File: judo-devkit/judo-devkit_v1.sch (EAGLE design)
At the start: 24 parts

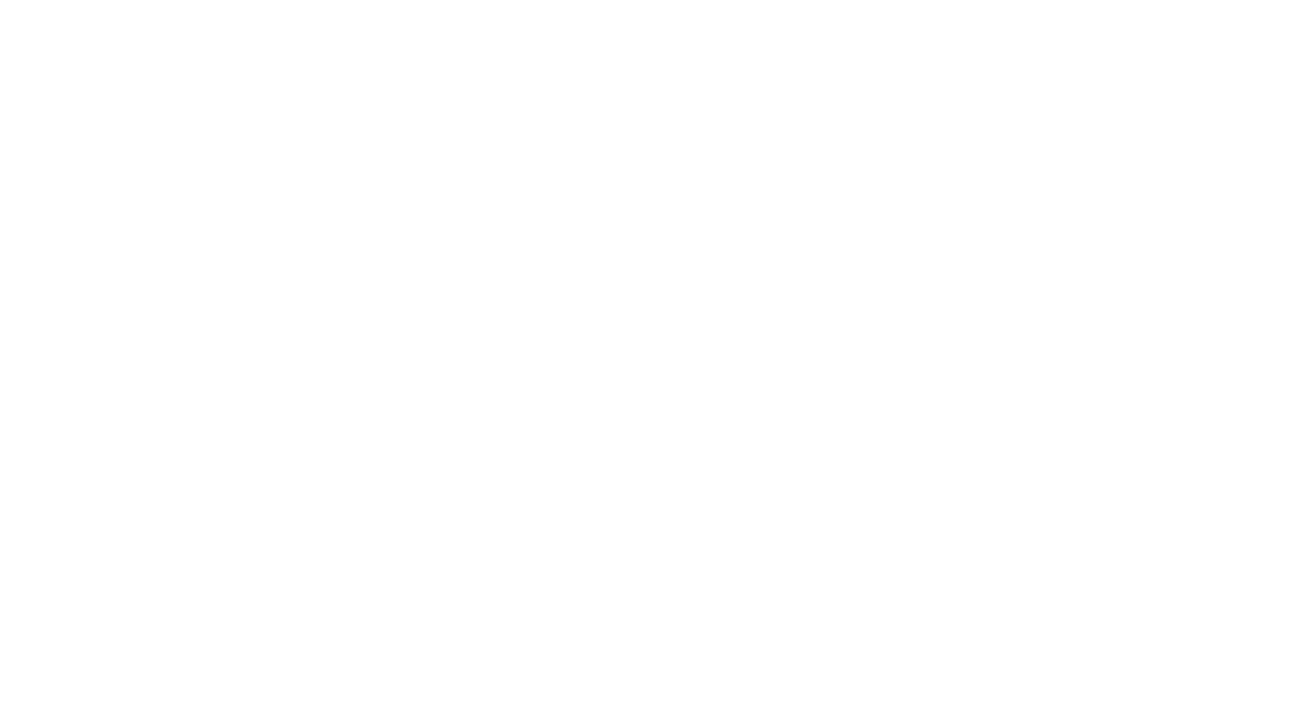
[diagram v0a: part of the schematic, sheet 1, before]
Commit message: added apollo3, power management
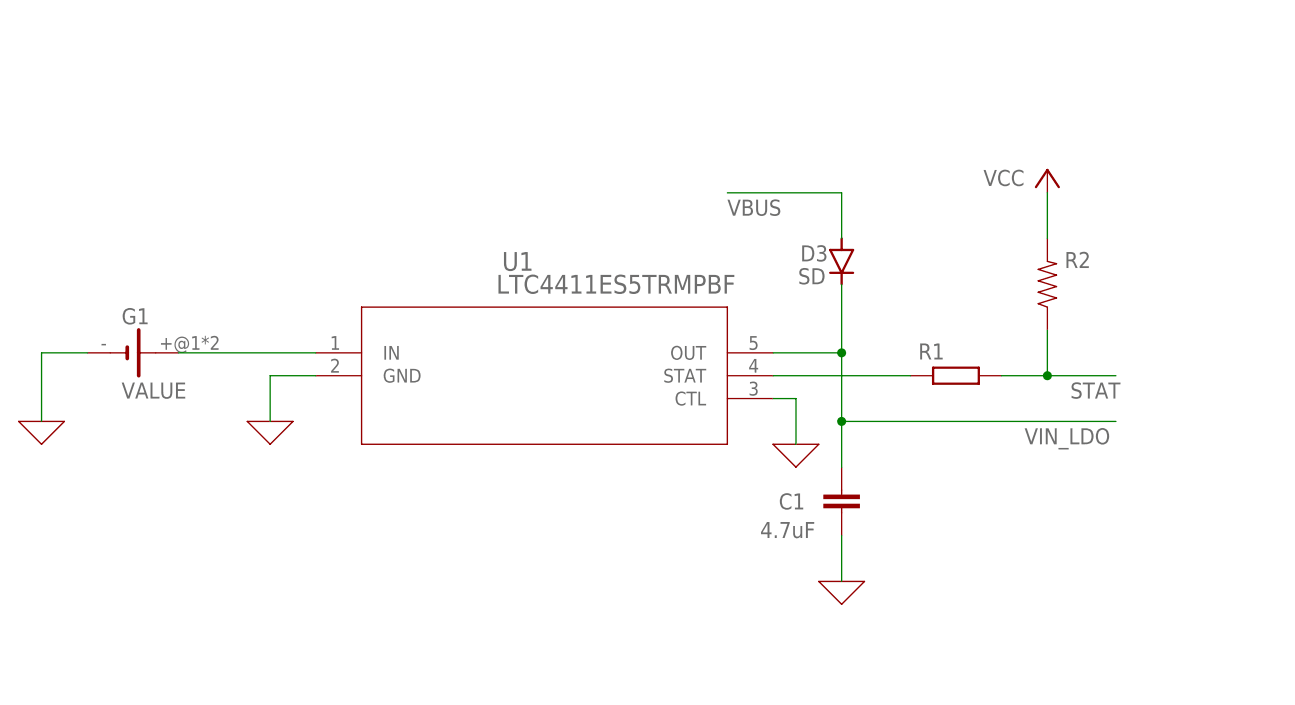
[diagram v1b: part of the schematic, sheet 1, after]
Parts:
- added C1: 4.7uF, Moo1.2:CAPACITOR
- added C13, C4: 15pF, SparkFun-Capacitors:15PF-0603-50V-5%
- added C14, C19: 0.1uF, SparkFun-Capacitors:0.1UF-0402T-16V-10%
- added C17: 10nF, SparkFun-Capacitors:10NF-0603-50V-10%
- added C18: 0.1uF, SparkFun-Capacitors:0.1UF-0603-25V-(+80/-20%)
- added C2, C23, C3: 1.0uF, SparkFun-Capacitors:1.0UF-0402T-16V-10%
- added C20, C21: 0.1uF, SparkFun-Capacitors:0.1UF-0603-25V-5%
- added C22: 10uF, SparkFun-Capacitors:10UF-0603-6.3V-20%
- added C28: 1nF, SparkFun-Capacitors:1.0NF/1000PF-0603-50V-10%
- added C5, C6: 4.7uF, SparkFun-Capacitors:4.7UF-0603-6.3V-(10%)
- added D10: GREEN, SparkFun-LED:LED-GREEN0603
- added D3: SD, diode:1N4148DO35-7
- added D4, D9: Yellow, SparkFun-LED:LED-YELLOW0603
- added D5, D7: 1A/23V/620mV, SparkFun-DiscreteSemi:DIODE-SCHOTTKY-BAT20J
- added D6: RED, SparkFun-LED:LED-RED0603
- added D8: BLUE, SparkFun-LED:LED-BLUE0603
- added E1: SPH0641LM4H, SparkFun-Sensors:SPH0641LM4H-1_MICROPHONE
- added FD1, FD2, FD3, FD4: FIDUCIALUFIDUCIAL, SparkFun-Aesthetics:FIDUCIALUFIDUCIAL
- added G1: 10MM_SM_COIN_CELL_CLIP, battery:10MM_SM_COIN_CELL_CLIP
- added J1: (no value), SparkFun-Connectors:JST_2MM_MALE
- added J10: USB Female Type C Connector, SparkFun-Connectors:USB_C4-LAYER-ISOLATED
- added J11: CORTEX_DEBUG, SparkFun-Connectors:CORTEX_JTAG_DEBUG_MINIMUM_PTH_NS
- added J12, J14, J4, J5: (no value), SparkFun-Connectors:CONN_021X02_NO_SILK
- added J13, J2: (no value), SparkFun-Connectors:CONN_12NO_SILK
- added J3: (no value), SparkFun-Connectors:QWIIC_CONNECTORJS-1MM
- added J7, J9: (no value), SparkFun-Connectors:CONN_07NO_SILK
- added R1: (no value), rcl:R-EU_R0402
- added R15, R16, R3, R6, R7: 1k, SparkFun-Resistors:1KOHM-0603-1/10W-1%
- added R17, R18: 5.1k, SparkFun-Resistors:5.1KOHM5.1KOHM-0603-1/10W-1%
- added R19: 220k, SparkFun-Resistors:220KOHM-0603-1/10W-1%
- added R2: (no value), SparkFun-Resistors:RESISTOR0805-RES
- added R20: DNP, SparkFun-Resistors:DNP-0603
- added R21: 100k, SparkFun-Resistors:100KOHM-0603-1/10W-1%
- added R4: 10k, SparkFun-Resistors:10KOHM-0603-1/10W-1%
- added R5: 2.0k, SparkFun-Resistors:2.0KOHM-0603-1/10W-5%
- added S1: RESET, SparkFun-Switches:MOMENTARY-SWITCH-SPST-SMD-4.6X2.8MM
- added TP1, TP2, TP3, TP4, TP5, TP6: TEST-POINT3X5, SparkFun-Connectors:TEST-POINT3X5
- added U1: LTC4411ES5TRMPBF, ltc4411:LTC4411ES5TRMPBF
- added U2: MCP73831, SparkFun-IC-Power:MCP73831
- added U3: 3.3V, SparkFun-IC-Power:V_REG_AP2112K-3.3V
- added U4: ARTEMIS_MODULESMD, SparkFun-IC-Microcontroller:ARTEMIS_MODULESMD
- added U6: CH340E_MSOP10, SparkFun-IC-Comms:CH340E_MSOP10
- added Y2: 32.768kHz, SparkFun-Clocks:CRYSTAL-32.768KHZSMD-3.2X1.5
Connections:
- new net !RESET: C20.2, C28.1, J11.!RESET, J2.10, R21.1, S1.2, U4.!RST
- new net !RTS: C20.1, C21.1, R20.2, U6.!RTS
- new net 10: J2.2, U4.(SDA4/MISO4/RX1)D40
- new net 3.3V: C14.1, C17.1, C18.1, C19.2, C22.1, C23.1, C3.1, E1.SEL, E1.VDD, J11.VCC, J2.9, J3.2, R15.2, R21.2, R3.2, R7.2, U3.OUT, U4.VDD*2, U6.V3, U6.VCC
- new net 8: J7.1, U4.(MOSI3/RX1)D38
- new net BOOT: C21.2, R19.2, U4.~BOOT(MOSI5/RX1/32KHZ)
- new net CC1: J10.CC1, R18.2
- new net CC2: J10.CC2, R17.2
- new net D+1: J10.D+, U6.UD+
- new net D-1: J10.D-, U6.UD-
- new net GND: C13.1, C14.2, C17.2, C18.2, C19.1, C2.2, C22.2, C23.2, C28.2, C3.2, C4.1, C5.2, C6.2, D6.C, D8.C, E1.GND, J1.-, J10.GND, J11.GND, J12.1, J13.1, J13.10, J13.11, J13.12, J13.2, J13.3, J13.4, J13.5, J13.6, J13.7, J13.8, J13.9, J14.1, J14.2, J2.11, J3.1, J4.2, J9.1, J9.2, J9.3, J9.4, J9.5, J9.6, J9.7, R17.1, R18.1, R19.1, R20.1, R5.1, S1.1, U2.VSS, U3.GND, U4.GND*6, U6.GND
- new net N$1: G1.+, U1.IN
- new net N$10: D6.A, R3.1
- new net N$11: D10.A, R7.1
- new net N$12: D9.A, R15.1
- new net N$2: R5.2, U2.PROG
- new net N$3: R1.2, U1.STAT
- new net N$4: D4.C, R6.2
- new net N$6: R6.1, U2.STAT
- new net N$7: C4.2, U4.XO, Y2.2
- new net N$8: C13.2, U4.XI, Y2.1
- new net N$9: D8.A, R16.1
- new net PDMCLK: E1.CLK, U4.(TX1/PDMCLK/SCCIO)~D37
- new net PDMDATA: E1.DATA, U4.(RX1/TRIG1/PDMDATA)D36
- new net RXI-0: D9.C, TP5.1, U4.~D49(RX0/SDA5/MISO5), U6.TXO
- new net SHLD: J10.SHLD
- new net STAT: R1.1, R2.1
- new net SWDCK: J11.SWDCLK, TP1.1, U4.D20(SWDCK/TX1)
- new net SWDIO: J11.SWDIO, TP2.1, U4.D21(SWDIO/RX1/SCCRST)
- new net TXO-0: D10.C, TP6.1, U4.~D48(TX0/SCL5/SCK5), U6.RXI
- new net VBUS: D3.A
- new net VCC: R2.2
- new net VIN: C2.1, D5.C, D7.C, J2.12, R4.2, U3.IN
- new net VIN_LDO: C1.2, D3.C, U1.OUT
- new net VREG_EN: J4.1, R4.1, U3.EN
- new net V_BATT: C6.1, D7.A, J1.+, J12.2, U2.VBAT
- new net V_USB: C5.1, D4.A, D5.A, J10.VBUS, U2.VIN
- new net ~11: J2.3, U4.(SCL0/SCK0)~D5
- new net ~12: J2.4, U4.(MOSI0/CLKOUT)~D7
- new net ~13: J2.5, U4.(SDA0/MISO0/I2SDAT)~D6
- new net ~4: J7.5, U4.(CMPIN1/SCCIO)~D18
- new net ~6: J7.3, U4.(SDA3/MISO3/RX1)~D43
- new net ~7: J7.2, U4.(SCL3/SCK3/TX1)~D42
- new net ~9: J2.1, U4.(SCL4/SCK4/TX1)~D39
- new net ~A0: J5.2, U4.~AD13(I2SBCLK/RX1)
- new net ~A1: J11.SWO, J5.1, U4.~AD33(SWO/32KHZ)
- new net ~A14: J2.6, U4.~AD35(TX1/I2SDAT/PDMCLK)
- new net ~A15: J2.7, U4.~AD32(SCCIO)
- new net ~A16: J2.8, U4.~AD12(PDMCLK/TX1)
- new net ~A2: J7.7, U4.~AD11(PDMDATA)
- new net ~A3: J7.6, U4.~AD29(PDMDATA)
- new net ~A5: J7.4, U4.~AD31(SCCCLK)
- new net ~D19/LED: R16.2, U4.(CMPRF0/SCCCLK/I2SBCLK)~D19
- new net ~D25/SDA2: J3.3, TP3.1, U4.(SDA2/MISO2/RX1)~D25
- new net ~D27/SCL2: J3.4, TP4.1, U4.(SCL2/SCK2)~D27
- net 0: now also C1.1, G1.-, U1.CTL, U1.GND
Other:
- note added: "3.3V Regulator"
- note added: "6V Max VIN / VUSB / VBATT"
- note added: "Artemis (Apollo3)"
- note added: "Artemis VCC Range: 1.76-3.6V"
- note added: "Bootloader Reset Circuit"
- note added: "Charge rate set to 500mA"
- note added: "Headers"
- note added: "I2C/Qwiic"
- note added: "Microphone"
- note added: "Power Source Select"
- note added: "SWD Program/Debug Interface"
- note added: "USB-to-Serial Converter"
- note added: "USB/LiPo Charger"
- note added: "User LED"

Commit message: updated apollo and power management
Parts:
- removed C10: (no value), rcl:CPOL-USCT3528
- removed C11: (no value), rcl:CPOL-USCT6032
- removed C12: (no value), rcl:CPOL-USCT7343
- removed C14: 0.1uF, SparkFun-Capacitors:0.1UF-0402T-16V-10%
- removed C9: (no value), rcl:CPOL-USCT3216
- removed D2: SD, diode:1N4148DO35-7
- removed D4: Yellow, SparkFun-LED:LED-YELLOW0603
- removed D5, D7: 1A/23V/620mV, SparkFun-DiscreteSemi:DIODE-SCHOTTKY-BAT20J
- removed D6: RED, SparkFun-LED:LED-RED0603
- removed E1: SPH0641LM4H, SparkFun-Sensors:SPH0641LM4H-1_MICROPHONE
- removed J12: (no value), SparkFun-Connectors:CONN_021X02_NO_SILK
- removed PD_VCC1: (no value), jumper:JP1E
- removed PHOTODIODE1: SLD-70BG2A, diode:1N4148DO35-7
- removed PHOTODIODE4: SLSD-71N300-ND, diode:1N4148DO35-7
- removed PHOTODIODE5: Radial, diode:1N4148DO35-7
- removed R1, R10, R11, R12, R13, R14: (no value), rcl:R-EU_R0402
- removed R3: 1k, SparkFun-Resistors:1KOHM-0603-1/10W-1%
- added JP1: (no value), jumper:JP2E
- added TP8: TEST-POINT3X5, SparkFun-Connectors:TEST-POINT3X5
- C5, C6: value 4.7uF -> 1.0uF; device SparkFun-Capacitors:4.7UF-0603-6.3V-(10%) -> SparkFun-Capacitors:1.0UF-0402T-16V-10%
- D1: value SD -> RED; device diode:1N4148DO35-7 -> SparkFun-LED:LED-RED0603
- D3: value SD -> 1A/23V/620mV; device diode:1N4148DO35-7 -> SparkFun-DiscreteSemi:DIODE-SCHOTTKY-BAT20J
- G1: value 10MM_SM_COIN_CELL_CLIP -> Coin Cell Holder; device battery:10MM_SM_COIN_CELL_CLIP -> SparkFun-Batteries:BATTERY-20MM_SMD_4LEGS
- J1: device SparkFun-Connectors:JST_2MM_MALE -> SparkFun-Connectors:CONN_021X02_NO_SILK
- R5: value 2.0k -> 1k; device SparkFun-Resistors:2.0KOHM-0603-1/10W-5% -> SparkFun-Resistors:1KOHM-0603-1/10W-1%
- R6: value 1k -> 10k; device SparkFun-Resistors:1KOHM-0603-1/10W-1% -> SparkFun-Resistors:10KOHM-0603-1/10W-1%
- R9: value (none) -> 0; device rcl:R-EU_R0402 -> SparkFun-Resistors:0OHM-0603-1/10W
- U1: MANUFACTURER_PART_NUMBER (none) -> LTC4411
- U2: value MCP73831 -> 3.3V; device SparkFun-IC-Power:MCP73831 -> SparkFun-IC-Power:V_REG_AP2112K-3.3V
- U3: value 3.3V -> AP2127K-1.8V; device SparkFun-IC-Power:V_REG_AP2112K-3.3V -> SparkFun-IC-Power:V_REG_AP2127K-1.8V
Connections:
- removed net 0: BASEBAND1.2, C1.1, C8.4, G1.-, TD3.4, TD_VCC1.2, TUNNELDIODE2.2, U1.CTL, U1.GND
- removed net D1+: PHOTODIODE1.C, R9.1
- removed net D1-: PHOTODIODE1.A, R12.1
- removed net D2+: PHOTODIODE4.C, R10.1
- removed net D2-: PHOTODIODE4.A, R13.1
- removed net D3+: PHOTODIODE5.C, R11.1
- removed net D3-: PHOTODIODE5.A, R14.1
- removed net IN+: C10.+, C11.+, C12.+, C9.+, D1.A, R10.2, R11.2, R9.2
- removed net IN-: C10.-, C11.-, C12.-, C9.-, D2.A, R12.2, R13.2, R14.2
- removed net N$10: D6.A, R3.1
- removed net N$4: D4.C, R6.2
- removed net N$6: R6.1, U2.STAT
- removed net VBUS: D3.A
- removed net VCC: R2.2
- removed net VIN+: D1.C, PD_VCC1.1
- removed net VIN-: D2.C, PD_VCC1.2
- removed net VIN_LDO: C1.2, D3.C, U1.OUT
- removed net V_BATT: C6.1, D7.A, J1.+, J12.2, U2.VBAT
- new net 1.8V: JP1.1, R2.2
- new net GND1: C5.2, C6.2, D1.C, U2.GND
- new net VDD: C19.2, C22.1, C23.1, J11.VCC, J2.9, J3.2, JP1.2, R21.2, U4.VDD*2
- new net VREG_EN1: J1.1, R6.1, U2.EN
- net 3.3V: now also C6.1, JP1.3, R16.2, R5.2, U2.OUT; no longer C14.1, C19.2, C22.1, C23.1, E1.SEL, E1.VDD, J11.VCC, J2.9, J3.2, R21.2, R3.2, U4.VDD*2
- net GND: now also BASEBAND1.2, C1.1, C8.4, G1.-, J1.2, TD3.4, TD_VCC1.2, TUNNELDIODE2.2, U1.CTL, U1.GND; no longer C14.2, C5.2, C6.2, D6.C, D8.C, E1.GND, J1.-, J12.1, R5.1, U2.VSS
- net N$2: now also D1.A, R5.1; no longer R5.2, U2.PROG
- net N$3: now also R9.1; no longer R1.2
- net PDMCLK: no longer E1.CLK
- net PDMDATA: no longer E1.DATA
- net STAT: now also R9.2, TP8.1; no longer R1.1
- net VIN: now also C1.2, D3.C, U1.OUT; no longer D5.C, D7.C
- net V_USB: now also D3.A, R6.2, U2.IN; no longer D4.A, D5.A, U2.VIN
- net ~D19/LED: now also D8.C; no longer R16.2
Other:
- note added: "1.8V Regulator"
- note added: "Battery and USB Power Management Circuit"
- note added: "Select Between 3.3V and 1.8V VDD"
- note removed: "6V Max VIN / VUSB / VBATT"
- note removed: "Charge rate set to 500mA"
- note removed: "Microphone"
- note removed: "Photo-Diodes and 0ohm Junctions"
- note removed: "Power Source Select"
- note removed: "Storage Bank"
- note removed: "USB/LiPo Charger"
- moved on the sheet: BASEBAND1, C1, C2, C3, C5, C6, C7, C8, IN2, J4, R2, R4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

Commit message: added sensors and cleaned up schematic
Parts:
- added R1, R10, R11, R3: 0, SparkFun-Resistors:0OHM-0603-1/10W
- added U5: BME280, microbuilder:BME280
- J10: device SparkFun-Connectors:USB_C4-LAYER-ISOLATED -> SparkFun-Connectors:USB_C_2-LAYER_PADS
- J3: value (none) -> QWIIC_RIGHT_ANGLE
- R2: value (none) -> 1k; device SparkFun-Resistors:RESISTOR0805-RES -> SparkFun-Resistors:1KOHM-0603-1/10W-1%
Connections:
- net 8 renamed ~8
- removed net GND1: C5.2, C6.2, D1.C, U2.GND
- new net N$14: R1.1, U5.SCK
- new net N$15: R10.1, U5.SDI
- new net N$4: R11.1, U5.CSB
- new net N$6: R3.1, U5.SDO
- new net ~MISO: R3.2, U4.(SDA0/MISO0/I2SDAT)~D6
- new net ~MOSI: R10.2, U4.(MOSI0/CLKOUT)~D7
- new net ~SCK: R1.2, U4.(SCL0/SCK0)~D5
- new net ~SPI_CS: R11.2, U4.(SCL1/SCK1/TX1/SCCLK)D8
- net 1.8V: now also C3.1, U3.OUT
- net 3.3V: no longer C3.1, U3.OUT
- net GND: now also C5.2, C6.2, D1.C, U2.GND, U5.GND
- net VDD: now also U5.VDD, U5.VDDIO
- net ~11: no longer U4.(SCL0/SCK0)~D5
- net ~12: no longer U4.(MOSI0/CLKOUT)~D7
- net ~13: no longer U4.(SDA0/MISO0/I2SDAT)~D6
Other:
- note added: "For I2C leave CSB pulled high (default value) SDI=SDA, SCK=SCL"
- note added: "For SPI set CSB low at startup SDO=MISO, SDI=MOSI, SCK=SCK, CSB=CS/SSEL"

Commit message: changed regulator
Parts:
- removed J4: (no value), SparkFun-Connectors:CONN_021X02_NO_SILK
- removed R4: 10k, SparkFun-Resistors:10KOHM-0603-1/10W-1%
- removed U3: AP2127K-1.8V, SparkFun-IC-Power:V_REG_AP2127K-1.8V
- added C10, C11: 7-30pF, SparkFun-Capacitors:CAP_ADJSMD
- added C12: .22F-SUPERCAP, SparkFun-Capacitors:.22F-SUPERCAP
- added C14, C9: 7pF, Moo1.2:CAPACITOR
- added C15: 1nF, Wurth_Capacitors_WCAP-CSST:WCAP-CSST_0805_885382207011
- added CFIL2, CFIL3: (no value), Moo1.2:0805_1
- added D2, D4, D5, D6: (no value), adafruit:DIODEDO-1N4148
- added H1, H2: MOUNT-HOLE2.8, holes:MOUNT-HOLE2.8
- added IN1: 6.8nH, Moo1.2:0603_1
- added JP2, JP3, JP4: (no value), jumper:JP1E
- added L1: 68uH, Wurth_Power Magnetics_WE-GFH:WE-GFH_3225_7447649168
- added REGULATOR: S-1313B20, customcomponents:S-1313B20
- added RSET1, RSET5, RSET6: 1k, rcl:R-US_R0603
- added S-8823A: S-8823A, customcomponents:S-8823A
- added S2: DIP-02-SMD-50MIL, SparkFun-Switches:DIP-02-SMD-50MIL
- added TUNNELDIODE1: BU-SMA-V, con-coax:BU-SMA-V
- added U$1: CUSTOMCOMPONENTS_S-1313B20, tunnelradio_02:CUSTOMCOMPONENTS_S-1313B20
- added VCC, VCC1, VCC2, VIN: TPPAD1-17, testpad:TPPAD1-17
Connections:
- removed net VREG_EN: J4.1, R4.1, U3.EN
- new net ANT1: C10.3, C9.2, TUNNELDIODE1.1
- new net BBIN: JP2.1, RSET1.2
- new net N$10: C14.2, C9.1
- new net N$13: D5.A, D6.C
- new net N$16: D4.A, D5.C, VCC1.TP
- new net N$17: D2.A, D4.C
- new net N$18: C14.1, IN1.2
- new net VBAT: C15.1, L1.2, S-8823A.CPOUT
- new net VCC: C3.1, CFIL3.1, D6.A, JP1.1, REGULATOR.VOUT, U$1.VOUT, VCC.TP
- new net VCC1: D2.C, RSET6.2, VIN.TP
- new net VHARSVT: S2.P$4
- new net VHARVST: S-8823A.OUT
- new net VIN1: CFIL2.1, REGULATOR.ONOFF, REGULATOR.VIN, S2.P$3
- new net VINHARVST: JP4.1, S-8823A.VIN
- net 1.8V: no longer C3.1, JP1.1, U3.OUT
- net GND: now also C10.4, C11.4, C12.+, C15.2, CFIL2.2, CFIL3.2, JP2.2, JP3.2, JP4.2, L1.1, REGULATOR.GND, REGULATOR.NC, RSET5.1, S-8823A.GND, S-8823A.ONOFF, TUNNELDIODE1.2, U$1.GND, U$1.NC; no longer J4.2, U3.GND
- net TDBIAS: now also C11.3, C12.-, IN1.1, RSET1.1, RSET5.2, RSET6.1, VCC2.TP
- net VIN: now also JP3.1, S2.P$1, S2.P$2, U$1.ONOFF, U$1.VIN; no longer R4.2, U3.IN
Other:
- note added: "Voltage Regulator"
- note removed: "1.8V Regulator"

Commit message: added board
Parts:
- removed C10, C11: 7-30pF, SparkFun-Capacitors:CAP_ADJSMD
- removed C12: .22F-SUPERCAP, SparkFun-Capacitors:.22F-SUPERCAP
- removed C14: 7pF, Moo1.2:CAPACITOR
- removed C15: 1nF, Wurth_Capacitors_WCAP-CSST:WCAP-CSST_0805_885382207011
- removed CFIL2, CFIL3: (no value), Moo1.2:0805_1
- removed D2, D4, D5, D6: (no value), adafruit:DIODEDO-1N4148
- removed H1, H2: MOUNT-HOLE2.8, holes:MOUNT-HOLE2.8
- removed IN1: 6.8nH, Moo1.2:0603_1
- removed JP2, JP3, JP4: (no value), jumper:JP1E
- removed L1: 68uH, Wurth_Power Magnetics_WE-GFH:WE-GFH_3225_7447649168
- removed REGULATOR: S-1313B20, customcomponents:S-1313B20
- removed RSET1, RSET5, RSET6: 1k, rcl:R-US_R0603
- removed S-8823A: S-8823A, customcomponents:S-8823A
- removed S2: DIP-02-SMD-50MIL, SparkFun-Switches:DIP-02-SMD-50MIL
- removed TUNNELDIODE1: BU-SMA-V, con-coax:BU-SMA-V
- removed VCC, VCC1, VCC2, VIN: TPPAD1-17, testpad:TPPAD1-17
- added CFIL1, CFIL4: (no value), Moo1.2:0805_1
- added H3, H4: MOUNT-HOLE2.8, holes:MOUNT-HOLE2.8
- added R12, R13, R4: 0, SparkFun-Resistors:0OHM-0603-1/10W
- added REGULATOR1: S-1313B20, customcomponents:S-1313B20
- added RSET2, RSET3: 1k, rcl:R-US_R0603
- added TDBIAS, TDBIAS_VCC, TDBIA_VCC: TPPAD1-17, testpad:TPPAD1-17
- C9: value 7pF -> (none); device Moo1.2:CAPACITOR -> SparkFun-Capacitors:CAP-0603
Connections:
- removed net 1.8V: R2.2
- removed net ANT1: C10.3, C9.2, TUNNELDIODE1.1
- removed net BBIN: JP2.1, RSET1.2
- removed net N$10: C14.2, C9.1
- removed net N$13: D5.A, D6.C
- removed net N$16: D4.A, D5.C, VCC1.TP
- removed net N$17: D2.A, D4.C
- removed net N$18: C14.1, IN1.2
- removed net RXI-0: D9.C, TP5.1, U4.~D49(RX0/SDA5/MISO5), U6.TXO
- removed net TXO-0: D10.C, TP6.1, U4.~D48(TX0/SCL5/SCK5), U6.RXI
- removed net VBAT: C15.1, L1.2, S-8823A.CPOUT
- removed net VCC1: D2.C, RSET6.2, VIN.TP
- removed net VHARSVT: S2.P$4
- removed net VHARVST: S-8823A.OUT
- removed net VIN1: CFIL2.1, REGULATOR.ONOFF, REGULATOR.VIN, S2.P$3
- removed net VINHARVST: JP4.1, S-8823A.VIN
- removed net ~11: J2.3
- removed net ~12: J2.4
- removed net ~13: J2.5
- new net BBIN_R: R13.1, U4.(SLMOSI/SLSDA)D1
- new net RXI-0_R: D9.C, R4.1, TP5.1, U6.TXO
- new net TDBIAS_VCC: CFIL4.1, REGULATOR1.VOUT, RSET3.2, TDBIAS_VCC.TP, TDBIA_VCC.TP
- new net TXO-0_R: D10.C, R12.1, TP6.1, U6.RXI
- new net ~RXI-0: R4.2, U4.~D49(RX0/SDA5/MISO5)
- new net ~TXO-0: R12.2, U4.~D48(TX0/SCL5/SCK5)
- net 3.3V: now also R21.2
- net BIN: now also C9.1, R13.2
- net GND: now also C9.2, CFIL1.1, CFIL4.2, REGULATOR1.GND, REGULATOR1.NC, RSET2.1; no longer C10.4, C11.4, C12.+, C15.2, CFIL2.2, CFIL3.2, JP2.2, JP3.2, JP4.2, L1.1, REGULATOR.GND, REGULATOR.NC, RSET5.1, S-8823A.GND, S-8823A.ONOFF, TUNNELDIODE1.2
- net PDMCLK: now also J2.3
- net PDMDATA: now also J2.4
- net TDBIAS: now also RSET2.2, RSET3.1, TDBIAS.TP; no longer C11.3, C12.-, IN1.1, RSET1.1, RSET5.2, RSET6.1, VCC2.TP
- net VCC: now also R2.2; no longer CFIL3.1, D6.A, REGULATOR.VOUT, VCC.TP
- net VDD: now also CFIL1.2, REGULATOR1.ONOFF, REGULATOR1.VIN; no longer R21.2
- net VIN: no longer JP3.1, S2.P$1, S2.P$2
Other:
- note added: "Jumpers for BB and TDBIAS"
- note added: "Mounting Holes"
- note added: "Select Between 3.3V and VCC"
- note added: "TDBIAS Voltage Divider"
- note added: "TDBIAS Voltage Regulator"
- note added: "Tunnel Diode Oscillator Circuit"
- note removed: "Select Between 3.3V and 1.8V VDD"
